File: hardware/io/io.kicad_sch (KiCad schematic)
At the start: 784 parts, among them J1 USB_B, J10 Conn_02x18_Odd_Even, J2 Conn_02x03_Odd_Even, J3 Conn_02x08_Odd_Even, J4 Conn_02x40_Odd_Even, J5 Conn_02x16_Odd_Even, J6 Conn_02x16_Odd_Even, J7 Conn_02x12_Odd_Even, J8 Conn_02x24_Odd_Even, J9 Barrel_Jack_MountingPin, Q129 IRLML6244, Q130 IRLML6402, Q131 IRLML6244, Q132 IRLML6402, Q133 IRLML6244, Q134 IRLML6402, Q135 IRLML6244, Q136 IRLML6402, Q137 IRLML6244, Q138 IRLML6402, Q139 IRLML6244, Q140 IRLML6402, Q141 IRLML6244, Q142 IRLML6402, Q143 IRLML6244, Q144 IRLML6402, Q145 IRLML6244, Q146 IRLML6402, Q147 IRLML6244, Q148 IRLML6402, Q149 IRLML6244, Q150 IRLML6402, Q151 IRLML6244, Q152 IRLML6402, Q153 IRLML6244, Q154 IRLML6402, Q155 IRLML6244, Q156 IRLML6402, Q157 IRLML6244, Q158 IRLML6402, Q159 IRLML6244, Q160 IRLML6402, Q161 IRLML6244, Q162 IRLML6402, Q163 IRLML6244, Q164 IRLML6402, Q165 IRLML6244, Q166 IRLML6402, Q167 IRLML6244, Q168 IRLML6402, Q169 IRLML6244, Q170 IRLML6402, Q171 IRLML6244, Q172 IRLML6402, Q173 IRLML6244, Q174 IRLML6402, Q175 IRLML6244, Q176 IRLML6402, Q177 IRLML6244, Q178 IRLML6402, Q179 IRLML6244, Q180 IRLML6402, Q181 IRLML6244, Q182 IRLML6402, Q183 IRLML6244, Q184 IRLML6402, Q185 IRLML6244, Q186 IRLML6402, Q187 IRLML6244, Q188 IRLML6402, Q189 IRLML6244, Q190 IRLML6402, Q191 IRLML6244, Q192 IRLML6402, Q193 IRLML6244, Q194 IRLML6402, Q195 IRLML6244, Q196 IRLML6402, Q197 IRLML6244, Q198 IRLML6402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

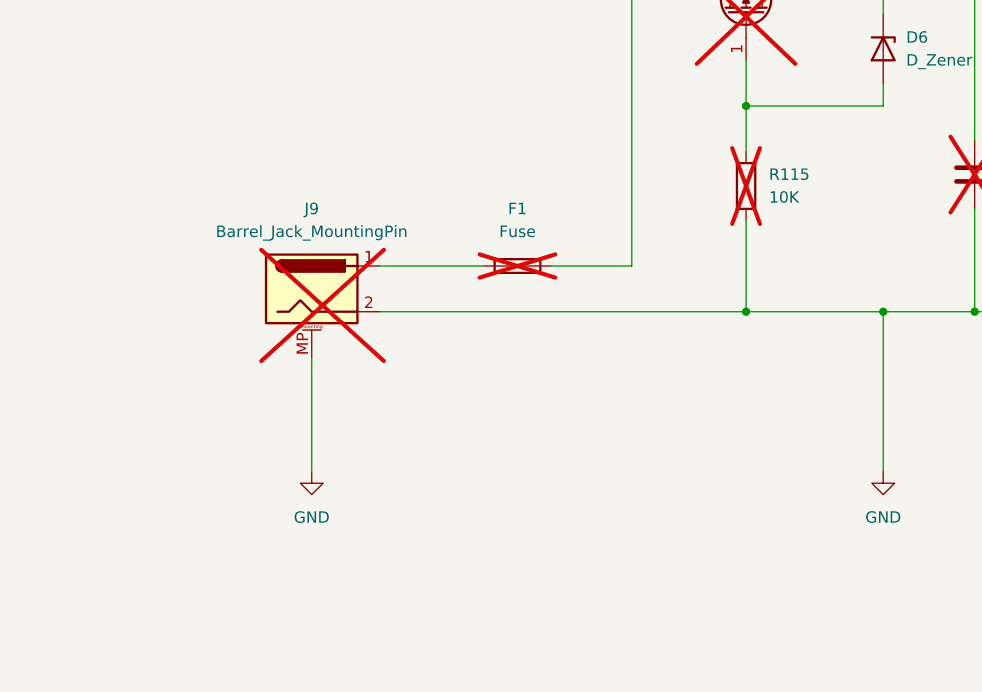
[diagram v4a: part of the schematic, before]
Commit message: large chunk of IO PCB routing is done
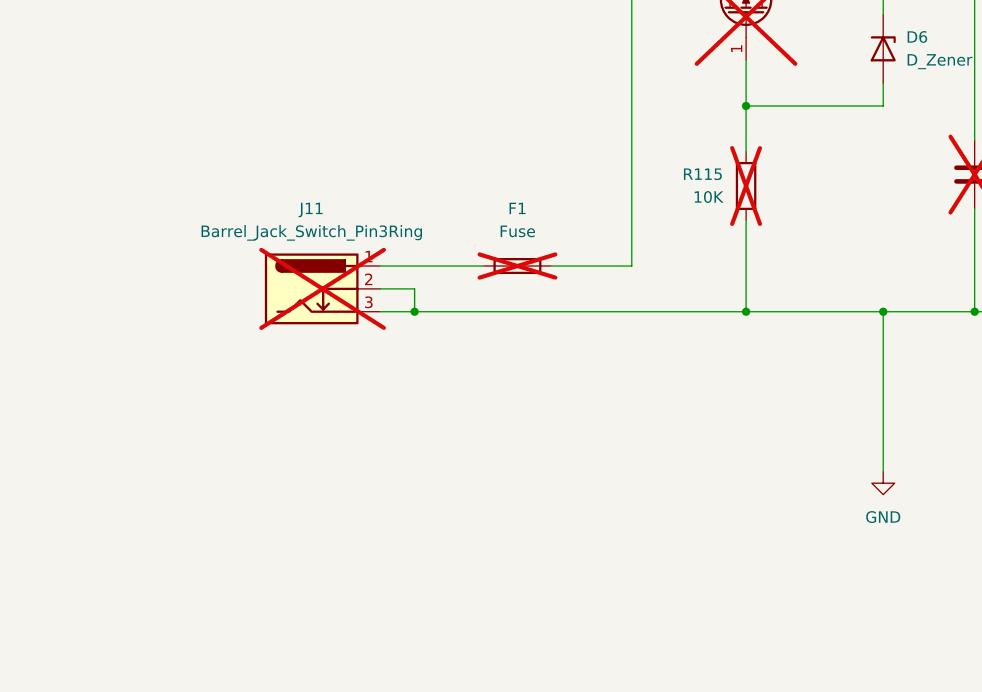
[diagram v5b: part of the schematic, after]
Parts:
- removed J9: Barrel_Jack_MountingPin, Connector_BarrelJack:BarrelJack_Horizontal, symbol Connector:Barrel_Jack_MountingPin
- added J11: Barrel_Jack_Switch_Pin3Ring, Connector_BarrelJack:BarrelJack_Horizontal, symbol Connector:Barrel_Jack_Switch_Pin3Ring
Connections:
- net GND: now also J11.2, J11.3
- net at F1.1: now also J11.1
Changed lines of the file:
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@@
 	)
 	(junction
+		(at 438.15 91.44)
+		(diameter 0)
+		(color 0 0 0 0)
+	)
+	(junction
 		(at 1193.8 869.95)
 		(diameter 0)
@@
 	(wire
 		(pts
+			(xy 438.15 91.44) (xy 474.98 91.44)
+		)
+		(stroke
+			(width 0)
+			(type default)
+		)
+	)
+	(wire
+		(pts
 			(xy 637.54 708.66) (xy 641.35 708.66)
 		)
@@
 	(wire
 		(pts
+			(xy 434.34 88.9) (xy 438.15 88.9)
+		)
+		(stroke
+			(width 0)
+			(type default)
+		)
+	)
+	(wire
+		(pts
 			(xy 800.1 1816.1) (xy 800.1 1807.21)
 		)
@@
 	(wire
 		(pts
+			(xy 438.15 88.9) (xy 438.15 91.44)
+		)
+		(stroke
+			(width 0)
+			(type default)
+		)
+	)
+	(wire
+		(pts
 			(xy 487.68 260.35) (xy 495.3 260.35)
 		)
@@
 	(wire
 		(pts
-			(xy 434.34 91.44) (xy 474.98 91.44)
+			(xy 434.34 91.44) (xy 438.15 91.44)
 		)
 		(stroke
@@
 	(wire
 		(pts
-			(xy 426.72 96.52) (xy 426.72 109.22)
-		)
-		(stroke
-			(width 0)
-			(type default)
-		)
-	)
-	(wire
-		(pts
 			(xy 1407.16 248.92) (xy 1418.59 248.92)
 		)
@@
 	)
 	(symbol
-		(lib_id "Connector:Barrel_Jack_MountingPin")
-		(at 426.72 88.9 0)
-		(unit 1)
-		(exclude_from_sim no)
-		(in_bom no)
-		(on_board yes)
-		(dnp yes)
-		(fields_autoplaced yes)
-		(property "Reference" "J9"
-			(at 426.72 80.01 0)
-			(effects
-				(font
-					(size 1.27 1.27)
-				)
-			)
-		)
-		(property "Value" "Barrel_Jack_MountingPin"
-			(at 426.72 82.55 0)
-			(effects
-				(font
-					(size 1.27 1.27)
-				)
-			)
-		)
-		(property "Footprint" "Connector_BarrelJack:BarrelJack_Horizontal"
-			(at 427.99 89.916 0)
-			(effects
-				(font
-					(size 1.27 1.27)
-				)
-				(hide yes)
-			)
-		)
-		(property "Datasheet" "~"
-			(at 427.99 89.916 0)
-			(effects
-				(font
-					(size 1.27 1.27)
-				)
-				(hide yes)
-			)
-		)
-		(property "Description" "DC Barrel Jack with a mounting pin"
-			(at 426.72 88.9 0)
-			(effects
-				(font
-					(size 1.27 1.27)
-				)
-				(hide yes)
-			)
-		)
-		(pin "2"
-		)
-		(pin "MP"
-		)
-		(pin "1"
-		)
-		(instances
-			(project ""
-				(path "/aaf6bf5a-f60a-4604-acad-8ada22c0fabd"
-					(reference "J9")
-					(unit 1)
-				)
-			)
-		)
-	)
-	(symbol
 		(lib_id "Device:R")
 		(at 1728.47 885.19 0)
@@
 	)
 	(symbol
+		(lib_id "Connector:Barrel_Jack_Switch_Pin3Ring")
+		(at 426.72 88.9 0)
+		(unit 1)
+		(exclude_from_sim no)
+		(in_bom no)
+		(on_board yes)
+		(dnp yes)
+		(fields_autoplaced yes)
+		(property "Reference" "J11"
+			(at 426.72 80.01 0)
+			(effects
+				(font
+					(size 1.27 1.27)
+				)
+			)
+		)
+		(property "Value" "Barrel_Jack_Switch_Pin3Ring"
+			(at 426.72 82.55 0)
+			(effects
+				(font
+					(size 1.27 1.27)
+				)
+			)
+		)
+		(property "Footprint" "Connector_BarrelJack:BarrelJack_Horizontal"
+			(at 427.99 89.916 0)
+			(effects
+				(font
+					(size 1.27 1.27)
+				)
+				(hide yes)
+			)
+		)
+		(property "Datasheet" "~"
+			(at 427.99 89.916 0)
+			(effects
+				(font
+					(size 1.27 1.27)
+				)
+				(hide yes)
+			)
+		)
+		(property "Description" "DC Barrel Jack with an internal switch"
+			(at 426.72 88.9 0)
+			(effects
+				(font
+					(size 1.27 1.27)
+				)
+				(hide yes)
+			)
+		)
+		(pin "2"
+		)
+		(pin "1"
+		)
+		(pin "3"
+		)
+		(instances
+			(project ""
+				(path "/aaf6bf5a-f60a-4604-acad-8ada22c0fabd"
+					(reference "J11")
+					(unit 1)
+				)
+			)
+		)
+	)
+	(symbol
 		(lib_id "Transistor_FET:IRLML6402")
 		(at 1004.57 798.83 0)
@@
 		(lib_id "Device:R")
 		(at 474.98 77.47 0)
+		(mirror y)
 		(unit 1)
 		(exclude_from_sim no)
@@
 		(on_board yes)
 		(dnp yes)
-		(fields_autoplaced yes)
 		(property "Reference" "R115"
-			(at 477.52 76.1999 0)
+			(at 472.44 76.1999 0)
 			(effects
 				(font
@@
 		)
 		(property "Value" "10K"
-			(at 477.52 78.7399 0)
+			(at 472.44 78.7399 0)
 			(effects
 				(font
@@
 		)
 		(property "Footprint" "Resistor_THT:R_Axial_DIN0207_L6.3mm_D2.5mm_P10.16mm_Horizontal"
-			(at 473.202 77.47 90)
+			(at 476.758 77.47 90)
 			(effects
 				(font
@@
 					(unit 1)
 				)
-			)
-		)
-	)
-	(symbol
-		(lib_id "power:GND")
-		(at 426.72 109.22 0)
-		(unit 1)
-		(exclude_from_sim no)
-		(in_bom yes)
-		(on_board yes)
-		(dnp no)
-		(fields_autoplaced yes)
-		(property "Reference" "#PWR0237"
-			(at 426.72 115.57 0)
-			(effects
-				(font
-					(size 1.27 1.27)
-				)
-				(hide yes)
-			)
-		)
-		(property "Value" "GND"
-			(at 426.72 114.3 0)
-			(effects
-				(font
-					(size 1.27 1.27)
-				)
-			)
-		)
-		(property "Footprint" ""
-			(at 426.72 109.22 0)
-			(effects
-				(font
-					(size 1.27 1.27)
-				)
-				(hide yes)
-			)
-		)
-		(property "Datasheet" ""
-			(at 426.72 109.22 0)
-			(effects
-				(font
-					(size 1.27 1.27)
-				)
-				(hide yes)
-			)
-		)
-		(property "Description" "Power symbol creates a global label with name \"GND\" , ground"
-			(at 426.72 109.22 0)
-			(effects
-				(font
-					(size 1.27 1.27)
-				)
-				(hide yes)
-			)
-		)
-		(pin "1"
-		)
-		(instances
-			(project "io"
-				(path "/aaf6bf5a-f60a-4604-acad-8ada22c0fabd"
-					(reference "#PWR0237")
-					(unit 1)
-				)
